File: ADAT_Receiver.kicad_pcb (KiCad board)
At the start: 2 copper layers, 52.1 x 26.7 mm, 21 parts, among them J1 USB_C_Receptacle_PowerOnly_6P, J2 PLR135-T, J3 Conn_01x07_Pin, J4 Conn_01x05_Pin, J5 PLx13xT, SW1 SW_DIP_x03, U1 V1402

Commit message: First order
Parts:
- SW1: footprint Button_Switch_SMD:SW_DIP_SPSTx03_Slide_6.7x9.18mm_W6.73mm_P2.54mm_LowProfile_JPin -> Button_Switch_SMD:SW_DIP_SPSTx03_Slide_6.7x9.18mm_W8.61mm_P2.54mm_LowProfile
- moved J4 10.2 mm to (117.9, 101.1), turned to 90 degrees
- moved SW1 1.02 mm to (109.5, 92.3)
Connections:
- J4 pad 2: IO0 -> DVCO
- J4 pad 3: IO1 -> IO2
- J4 pad 4: IO2 -> IO1
- J4 pad 5: DVCO -> IO0
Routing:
- net (no net): track 38.5 -> 0.00 mm
- net DVCO: track 0.00 -> 16.6 mm
- net IO2: track 0.00 -> 12.3 mm
- net IO1: track 0.00 -> 9.65 mm
- net /ERR: track 34.0 -> 27.1 mm
- net IO0: track 0.00 -> 6.94 mm
- net VDD: track 62.9 -> 59.5 mm
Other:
- board text added: "JLCJLCJLCJLC"

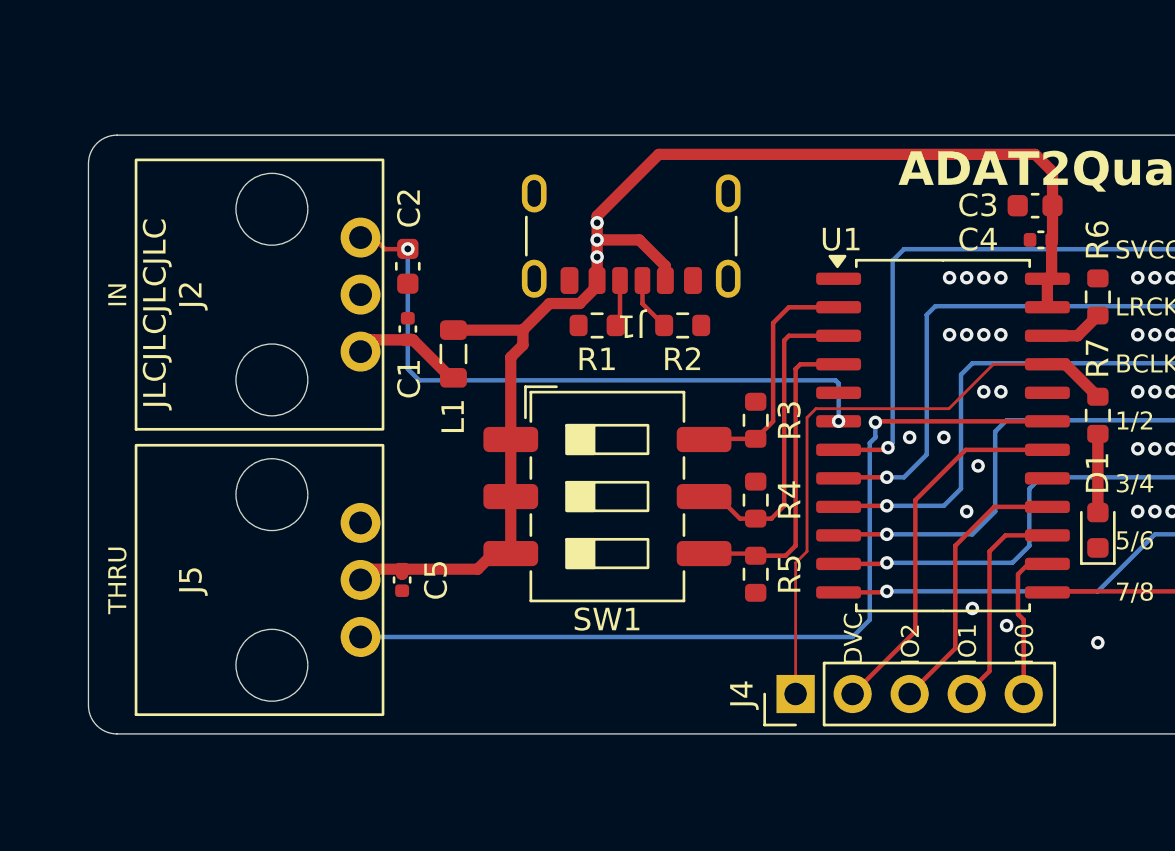
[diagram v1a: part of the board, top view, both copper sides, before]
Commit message: Fixed photolink receiver pin assign
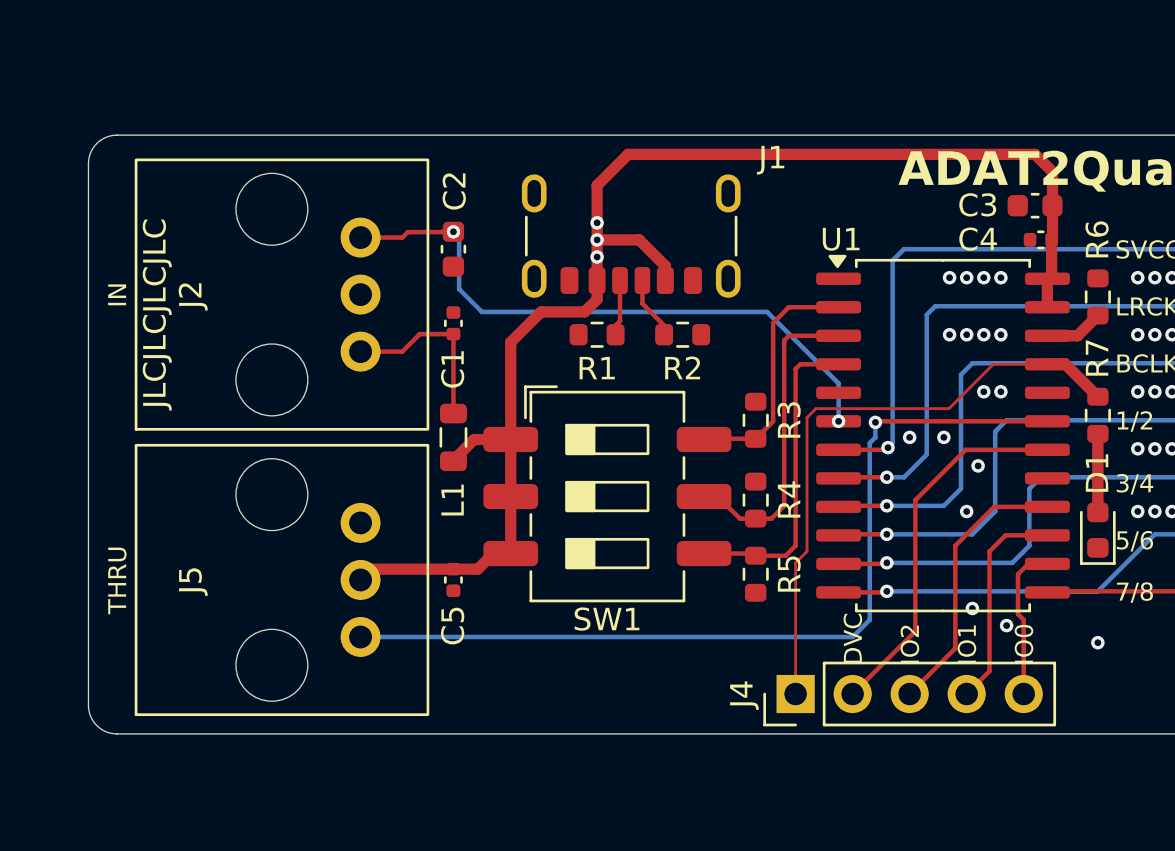
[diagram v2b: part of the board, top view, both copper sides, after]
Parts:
- J2: value PLR135-T -> PLR135/T
- J5: value PLx13xT -> PLT133/T
- moved L1 3.72 mm to (102.6, 89.7), turned to 90 degrees
- moved C5 2.29 mm to (102.6, 96.0)
- moved C2 2.17 mm to (102.6, 81.3)
- moved C1 2.05 mm to (102.6, 84.6)
- moved R1 0.41 mm to (109.0, 85.1)
- moved R2 0.41 mm to (112.8, 85.1)
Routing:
- net Net-(J2-Vcc): track 5.06 -> 8.00 mm
- net Net-(J2-Vout): track 28.8 -> 27.2 mm
- net VDD: track 59.5 -> 60.5 mm
